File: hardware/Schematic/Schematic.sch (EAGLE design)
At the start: 2 parts

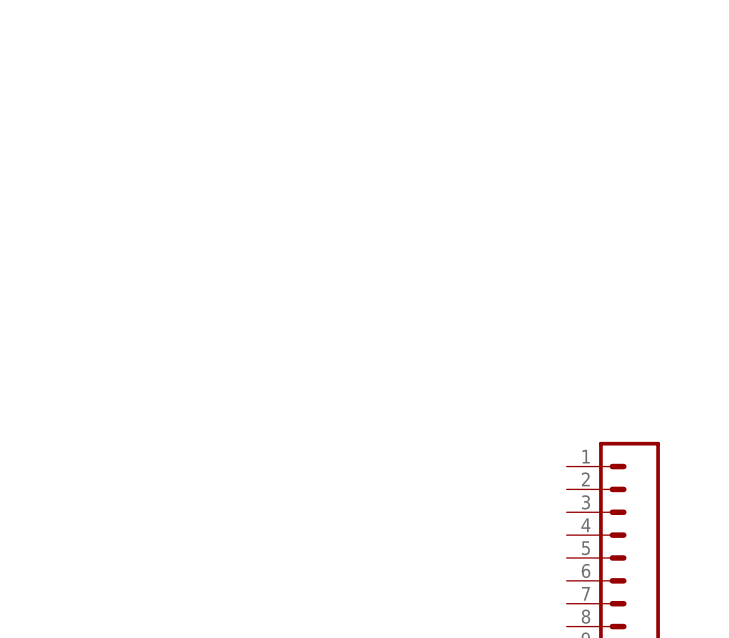
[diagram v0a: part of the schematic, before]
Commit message: created symbol for the mosfet and added it to the schematic
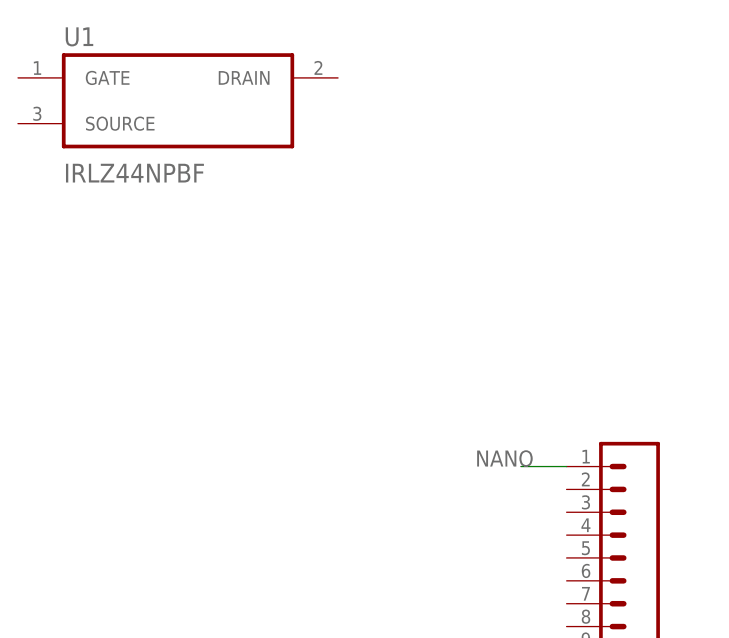
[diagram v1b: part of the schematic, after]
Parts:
- added U1: IRLZ44NPBF, IRLZ44NPBF:IRLZ44NPBF
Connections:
- new net NANO: J1.1
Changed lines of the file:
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@@
 <part name="J2" library="SparkFun-Connectors" deviceset="CONN_15" device=""/>
 <part name="FRAME1" library="frames" library_urn="urn:adsk.eagle:library:229" deviceset="A3L-LOC" device=""/>
+<part name="U1" library="IRLZ44NPBF" deviceset="IRLZ44NPBF" device=""/>
 </parts>
 <sheets>
@@
 <attribute name="SHEET" x="377.825" y="50.8" size="2.54" layer="94"/>
 </instance>
+<instance part="U1" gate="G$1" x="137.16" y="243.84" smashed="yes">
+<attribute name="NAME" x="124.46" y="249.92" size="2.0828" layer="95" ratio="10" rot="SR0"/>
+<attribute name="VALUE" x="124.46" y="234.76" size="2.0828" layer="96" ratio="10" rot="SR0"/>
+</instance>
 </instances>
 <busses>
@@
 </segment>
 </net>
+<net name="NANO" class="0">
+<segment>
+<pinref part="J1" gate="G$1" pin="1"/>
+<wire x1="180.34" y1="203.2" x2="175.26" y2="203.2" width="0.1524" layer="91"/>
+<label x="170.18" y="203.2" size="1.778" layer="95"/>
+</segment>
+</net>

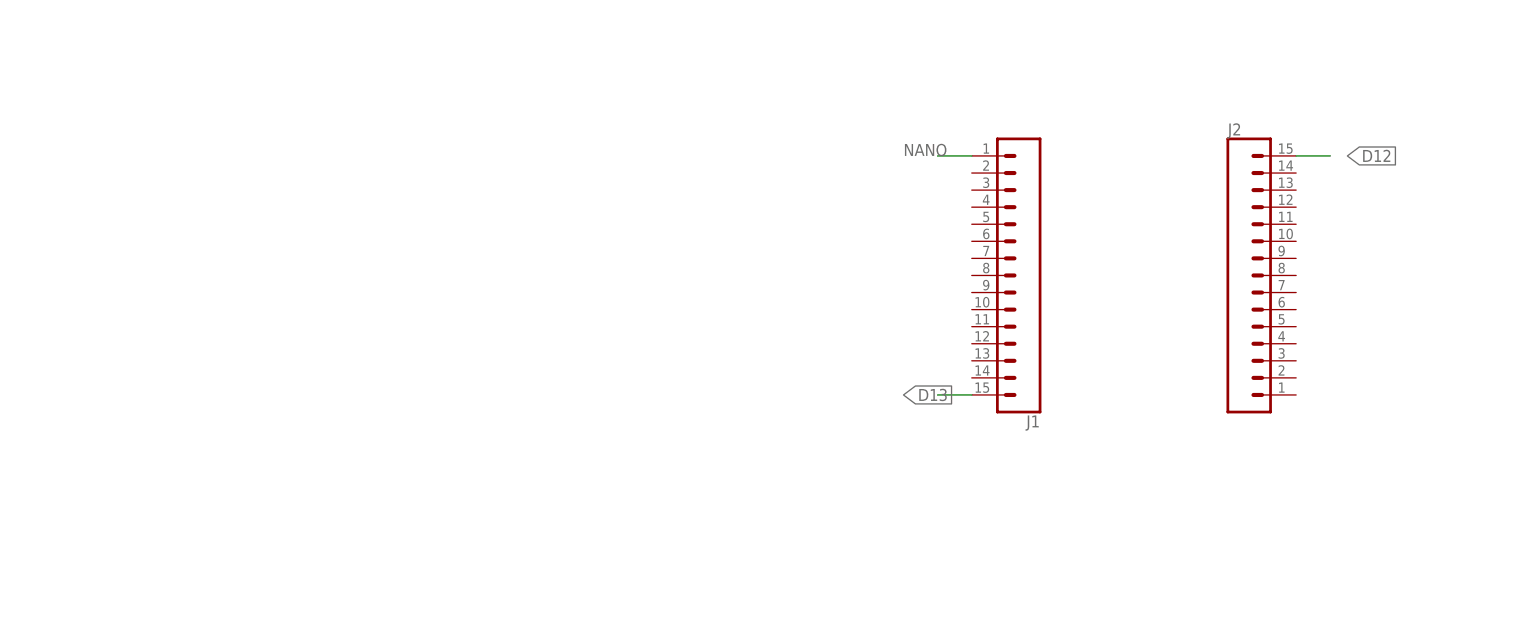
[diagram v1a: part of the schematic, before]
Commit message: added the open pins in the schematic for the buck converter
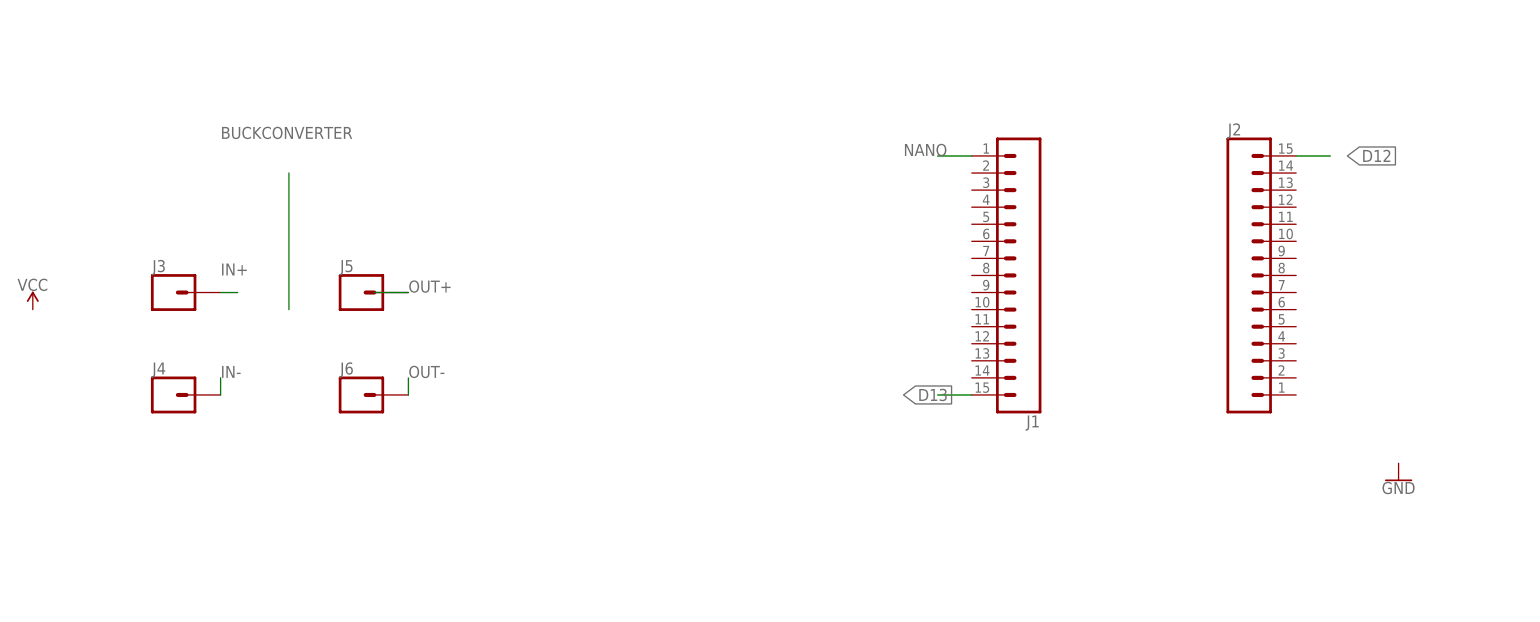
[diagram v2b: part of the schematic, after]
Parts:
- added J3, J4, J5, J6: (no value), SparkFun-Connectors:CONN_01
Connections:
- new net IN+: J3.1
- new net IN-: J4.1
- new net OUT+: J5.1
- new net OUT-: J6.1
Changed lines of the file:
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@@
 <part name="FRAME1" library="frames" library_urn="urn:adsk.eagle:library:229" deviceset="A3L-LOC" device=""/>
 <part name="U1" library="IRLZ44NPBF" deviceset="IRLZ44NPBF" device=""/>
+<part name="J3" library="SparkFun-Connectors" deviceset="CONN_01" device=""/>
+<part name="J4" library="SparkFun-Connectors" deviceset="CONN_01" device=""/>
+<part name="J5" library="SparkFun-Connectors" deviceset="CONN_01" device=""/>
+<part name="J6" library="SparkFun-Connectors" deviceset="CONN_01" device=""/>
+<part name="GND1" library="SparkFun-PowerSymbols" deviceset="GND" device=""/>
+<part name="SUPPLY1" library="SparkFun-PowerSymbols" deviceset="VCC" device=""/>
 </parts>
 <sheets>
@@
 <attribute name="NAME" x="124.46" y="249.92" size="2.0828" layer="95" ratio="10" rot="SR0"/>
 <attribute name="VALUE" x="124.46" y="234.76" size="2.0828" layer="96" ratio="10" rot="SR0"/>
+</instance>
+<instance part="J3" gate="J1" x="60.96" y="182.88" smashed="yes">
+<attribute name="VALUE" x="58.42" y="178.054" size="1.778" layer="96" font="vector"/>
+<attribute name="NAME" x="58.42" y="185.928" size="1.778" layer="95" font="vector"/>
+</instance>
+<instance part="J4" gate="J1" x="60.96" y="167.64" smashed="yes">
+<attribute name="VALUE" x="58.42" y="162.814" size="1.778" layer="96" font="vector"/>
+<attribute name="NAME" x="58.42" y="170.688" size="1.778" layer="95" font="vector"/>
+</instance>
+<instance part="J5" gate="J1" x="88.9" y="182.88" smashed="yes">
+<attribute name="VALUE" x="86.36" y="178.054" size="1.778" layer="96" font="vector"/>
+<attribute name="NAME" x="86.36" y="185.928" size="1.778" layer="95" font="vector"/>
+</instance>
+<instance part="J6" gate="J1" x="88.9" y="167.64" smashed="yes">
+<attribute name="VALUE" x="86.36" y="162.814" size="1.778" layer="96" font="vector"/>
+<attribute name="NAME" x="86.36" y="170.688" size="1.778" layer="95" font="vector"/>
+</instance>
+<instance part="GND1" gate="1" x="243.84" y="154.94" smashed="yes">
+<attribute name="VALUE" x="243.84" y="154.686" size="1.778" layer="96" font="vector" align="top-center"/>
+</instance>
+<instance part="SUPPLY1" gate="G$1" x="40.64" y="180.34" smashed="yes">
+<attribute name="VALUE" x="40.64" y="183.134" size="1.778" layer="96" font="vector" align="bottom-center"/>
 </instance>
 </instances>
@@
 </segment>
 </net>
+<net name="BUCKCONVERTER" class="0">
+<segment>
+<wire x1="78.74" y1="180.34" x2="78.74" y2="200.66" width="0.1524" layer="91"/>
+<label x="68.58" y="205.74" size="1.778" layer="95"/>
+</segment>
+</net>
+<net name="OUT+" class="0">
+<segment>
+<pinref part="J5" gate="J1" pin="1"/>
+<wire x1="96.52" y1="182.88" x2="91.44" y2="182.88" width="0.1524" layer="91"/>
+<label x="96.52" y="182.88" size="1.778" layer="95"/>
+</segment>
+</net>
+<net name="OUT-" class="0">
+<segment>
+<pinref part="J6" gate="J1" pin="1"/>
+<wire x1="96.52" y1="167.64" x2="96.52" y2="170.18" width="0.1524" layer="91"/>
+<label x="96.52" y="170.18" size="1.778" layer="95"/>
+</segment>
+</net>
+<net name="IN-" class="0">
+<segment>
+<pinref part="J4" gate="J1" pin="1"/>
+<wire x1="68.58" y1="167.64" x2="68.58" y2="170.18" width="0.1524" layer="91"/>
+<label x="68.58" y="170.18" size="1.778" layer="95"/>
+</segment>
+</net>
+<net name="IN+" class="0">
+<segment>
+<pinref part="J3" gate="J1" pin="1"/>
+<wire x1="68.58" y1="182.88" x2="71.12" y2="182.88" width="0.1524" layer="91"/>
+<label x="68.58" y="185.42" size="1.778" layer="95"/>
+</segment>
+</net>
